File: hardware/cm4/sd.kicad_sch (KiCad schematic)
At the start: 5 parts, among them J13 microSD, U11 AP22804AW5

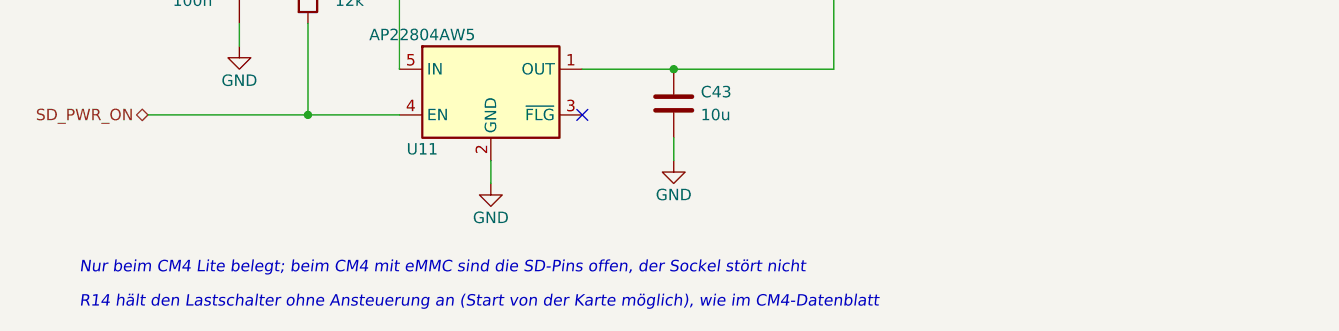
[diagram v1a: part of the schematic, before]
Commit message: Schaltplan: Hinweise als Textkästen (KiCad bricht um); Texte werden in den Generator zurückgeführt
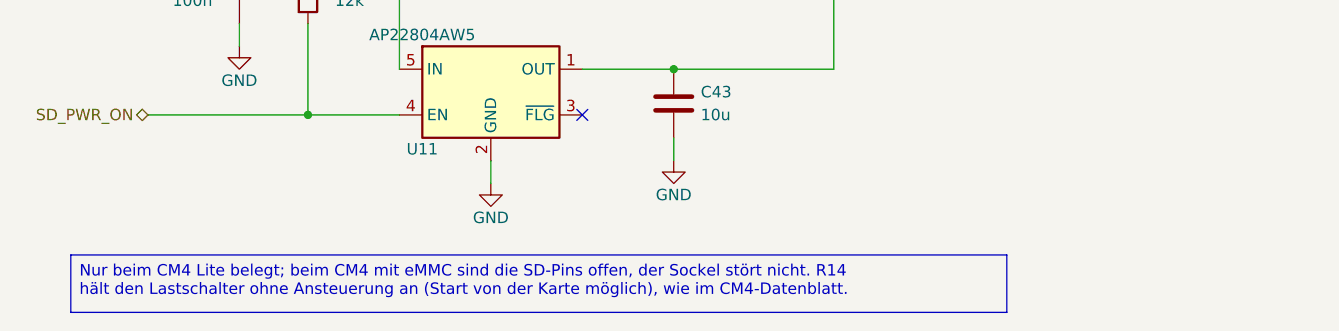
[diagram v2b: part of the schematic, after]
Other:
- note removed: "Nur beim CM4 Lite belegt; beim CM4 mit eMMC sind die SD-Pins offen, der Sockel stört nicht"
- note removed: "R14 hält den Lastschalter ohne Ansteuerung an (Start von der Karte möglich), wie im CM4-Datenblatt"
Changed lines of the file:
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@@
 	(hierarchical_label "SD_DAT1" (shape bidirectional) (at 213.36 118.11 180) (effects (font (size 1.27 1.27)) (justify right)))
 	(hierarchical_label "SD_PWR_ON" (shape bidirectional) (at 144.78 148.59 180) (effects (font (size 1.27 1.27)) (justify right)))
-	(text "Nur beim CM4 Lite belegt; beim CM4 mit eMMC sind die SD-Pins offen, der Sockel stört nicht" (exclude_from_sim no) (at 137.16 166.37 0) (effects (font (size 1.27 1.27) italic) (justify left bottom)))
-	(text "R14 hält den Lastschalter ohne Ansteuerung an (Start von der Karte möglich), wie im CM4-Datenblatt" (exclude_from_sim no) (at 137.16 170.18 0) (effects (font (size 1.27 1.27) italic) (justify left bottom)))
+	(text_box "Nur beim CM4 Lite belegt; beim CM4 mit eMMC sind die SD-Pins offen, der Sockel stört nicht. R14 hält den Lastschalter ohne Ansteuerung an (Start von der Karte möglich), wie im CM4-Datenblatt." (exclude_from_sim no) (at 136.21 164.15 0) (size 104 6.38) (margins 0.9525 0.9525 0.9525 0.9525) (stroke (width 0.1) (type solid) (color 132 132 132 1)) (fill (type color) (color 255 255 230 1)) (effects (font (size 1.27 1.27)) (justify left top)))
 	(embedded_fonts no)
 )
